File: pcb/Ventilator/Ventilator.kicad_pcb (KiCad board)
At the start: 2 copper layers, 91 parts, among them J2 Screw_Terminal_01x08, J3 Screw_Terminal_01x08, J4 Screw_Terminal_01x02, K1 FINDER-40.52.7.012.0000, K2 FINDER-40.52.7.012.0000, K3 FINDER-40.52.7.012.0000, Q1 NUD3160, Q2 NUD3160, Q3 NUD3160, SW1 Reset, U1 W25Q128JVS, U2 RP2040, U3 4N25, U4 4N25, U5 4N25, U6 4N25, U7 NCP1117-3.3_SOT223

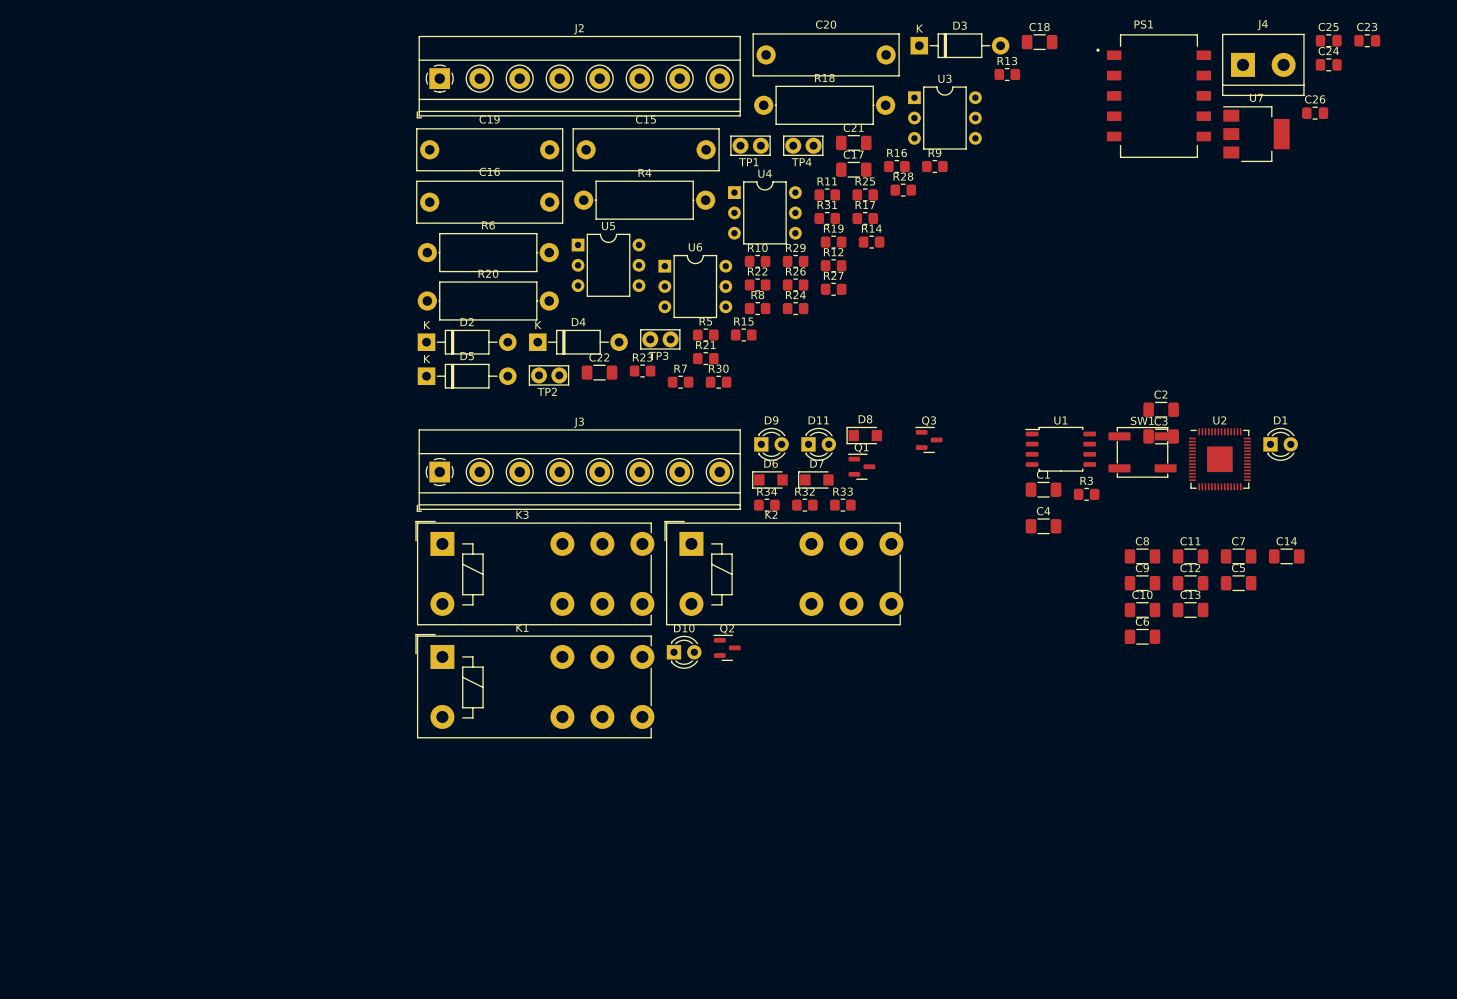
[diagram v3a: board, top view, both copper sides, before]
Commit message: - all parts connected, placed partially
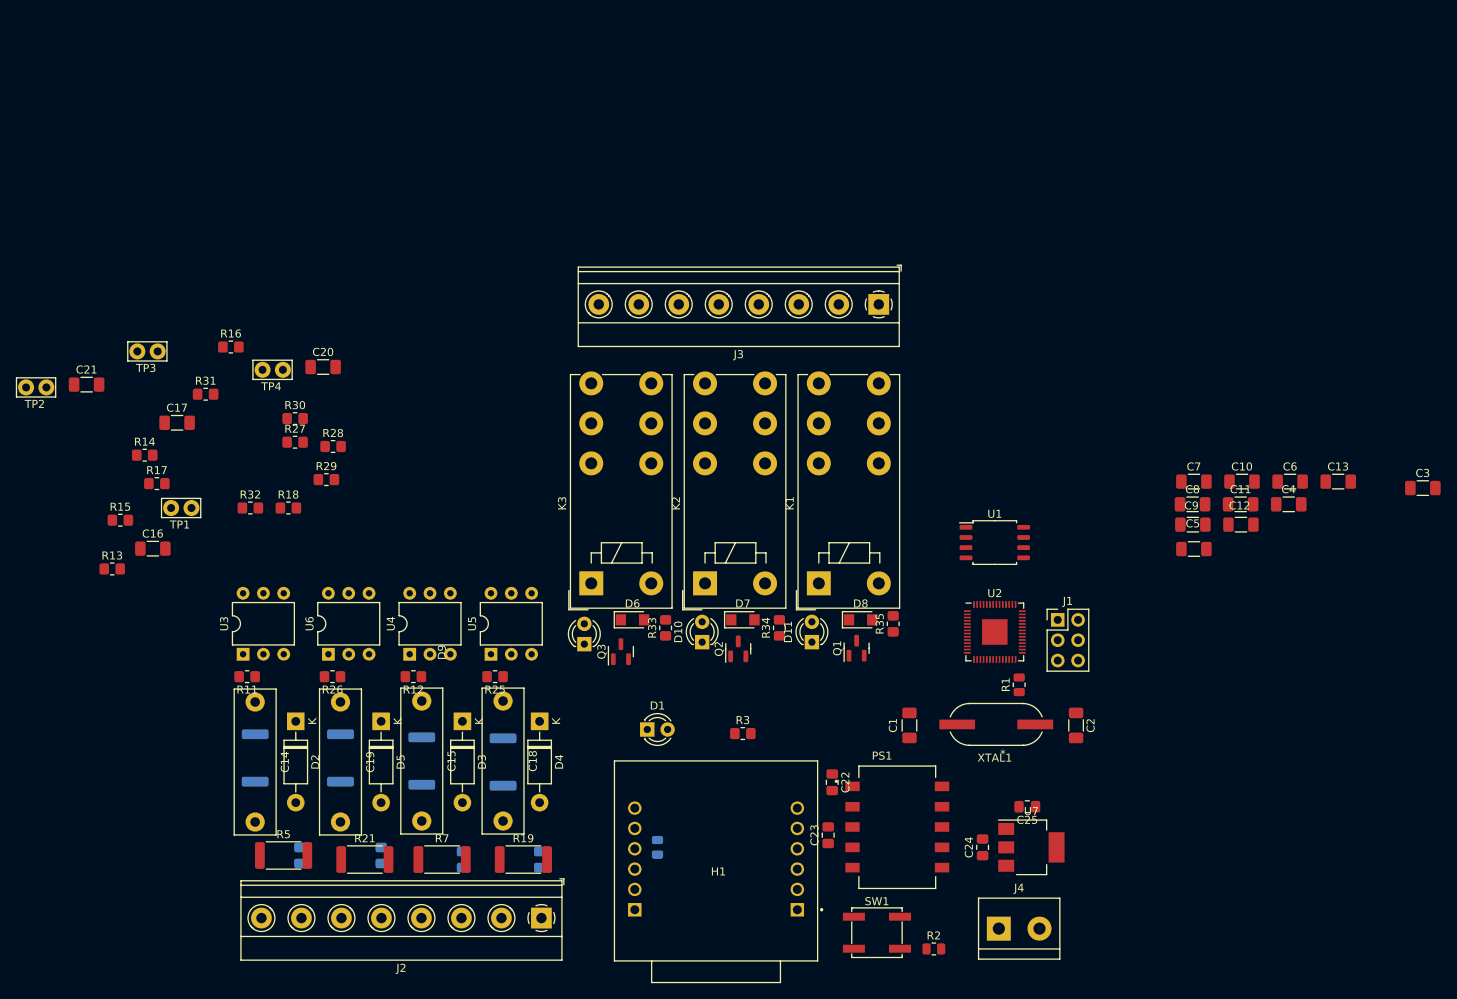
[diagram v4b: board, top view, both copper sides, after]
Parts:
- removed the C1 at (140.2, 127.0)
- added H1: WIZ850IO, W5500:WIZ850IO, F.Cu at (99.6, 174.8)
- added J1: Conn_02x03_Top_Bottom, Connector_PinHeader_2.54mm:PinHeader_2x03_P2.54mm_Vertical, F.Cu at (142.0, 143.3)
- added R1: 1k, Resistor_SMD:R_0805_2012Metric, F.Cu at (137.2, 151.4)
- added R2: 1k, Resistor_SMD:R_0805_2012Metric, F.Cu at (126.5, 184.4)
- added R4: 10k, Resistor_SMD:R_0805_2012Metric, B.Cu at (91.9, 171.7)
- added XTAL1: , Xtal:ABLS-12.000MHZ-B4-T, F.Cu at (134.3, 156.3)
- R10: renamed from R9; footprint Resistor_SMD:R_0805_2012Metric_Pad1.20x1.40mm_HandSolder -> Resistor_SMD:R_2512_6332Metric; moved to B.Cu
- R19: renamed from R18; footprint Resistor_THT:R_Axial_DIN0414_L11.9mm_D4.5mm_P15.24mm_Horizontal -> Resistor_SMD:R_2512_6332Metric
- R20: renamed from R19; moved to B.Cu
- R21: renamed from R20; footprint Resistor_THT:R_Axial_DIN0414_L11.9mm_D4.5mm_P15.24mm_Horizontal -> Resistor_SMD:R_2512_6332Metric
- R22: renamed from R21; moved to B.Cu
- R23: renamed from R22; footprint Resistor_SMD:R_0805_2012Metric_Pad1.20x1.40mm_HandSolder -> Resistor_SMD:R_2512_6332Metric; moved to B.Cu
- R24: renamed from R23; footprint Resistor_SMD:R_0805_2012Metric_Pad1.20x1.40mm_HandSolder -> Resistor_SMD:R_2512_6332Metric; moved to B.Cu
- R5: renamed from R4; footprint Resistor_THT:R_Axial_DIN0414_L11.9mm_D4.5mm_P15.24mm_Horizontal -> Resistor_SMD:R_2512_6332Metric
- R6: renamed from R5; moved to B.Cu
- R7: renamed from R6; footprint Resistor_THT:R_Axial_DIN0414_L11.9mm_D4.5mm_P15.24mm_Horizontal -> Resistor_SMD:R_2512_6332Metric
- R8: renamed from R7; moved to B.Cu
- R9: renamed from R8; footprint Resistor_SMD:R_0805_2012Metric_Pad1.20x1.40mm_HandSolder -> Resistor_SMD:R_2512_6332Metric; moved to B.Cu
- moved R14 117.8 mm to (27.9, 122.7)
- moved C17 117.8 mm to (31.9, 118.6)
- moved C23 114.8 mm to (113.3, 170.2), turned to 90 degrees
- moved C22 114.3 mm to (113.8, 163.6), turned to -90 degrees
- moved J4 112.2 mm to (134.6, 181.9)
- moved C24 109.7 mm to (132.6, 171.7), turned to 90 degrees
- moved U3 109.0 mm to (40.1, 147.6), turned to 90 degrees
- moved J2 105.7 mm to (77.4, 180.5), turned to 180 degrees
- moved D3 102.0 mm to (67.6, 156.0), turned to -90 degrees
- moved R17 100.6 mm to (29.4, 126.2)
- moved R15 100.1 mm to (24.8, 130.8)
- moved C16 99.6 mm to (28.9, 134.4)
- moved R19 98.9 mm to (75.2, 173.2)
- moved R10 98.2 mm to (62.5, 160.9), turned to -90 degrees
- moved R13 97.8 mm to (23.8, 136.9)
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- renumbered C2 to C1, C11 to C10, C12 to C11, C13 to C12, C14 to C13, C15 to C14, C16 to C15, C17 to C16, C18 to C17, C19 to C18, C20 to C19, C3 to C2, C21 to C20, C22 to C21, C23 to C22, C24 to C23, C25 to C24, C26 to C25, C4 to C3, C5 to C4, C6 to C5, C7 to C6, C8 to C7, C9 to C8, C10 to C9, R10 to R11, R11 to R12, R12 to R13, R13 to R14, R14 to R15, R15 to R16, R16 to R17, R17 to R18, R24 to R25, R25 to R26, R26 to R27, R27 to R28, R28 to R29, R29 to R30, R30 to R31, R31 to R32, R32 to R33, R33 to R34, R34 to R35
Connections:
- C22 pad 1: Net-(C23-Pad1) -> +12V
- D10 pad 2: VCC -> +12V
- D11 pad 2: VCC -> +12V
- D6 pad 1: VCC -> +12V
- D7 pad 1: VCC -> +12V
- D8 pad 1: VCC -> +12V
- D9 pad 2: VCC -> +12V
- J4 pad 2: Net-(C23-Pad1) -> +12V
- K1 pad A1: VCC -> +12V
- K2 pad A1: VCC -> +12V
- K3 pad A1: VCC -> +12V
- PS1 pad 1: Net-(C23-Pad1) -> +12V
- PS1 pad 2: Net-(C23-Pad1) -> +12V
- U2 pad 24: unconnected-(U2-Pad24) -> /CPU/SWCLK
- U2 pad 25: unconnected-(U2-Pad25) -> /CPU/SWD
- U2 pad 27: unconnected-(U2-Pad27) -> /CPU/MISO
- U2 pad 28: unconnected-(U2-Pad28) -> /CPU/SCNN
- U2 pad 29: unconnected-(U2-Pad29) -> /CPU/SCLK
- U2 pad 3: unconnected-(U2-Pad3) -> /CPU/RX
- U2 pad 30: unconnected-(U2-Pad30) -> /CPU/MOSI
- U2 pad 31: unconnected-(U2-Pad31) -> /CPU/RSTN

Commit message: - voor omschakeling naar rp pico
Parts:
- removed the C10 at (165.0, 126.0)
- added D12: BAT760,115, Diode_SMD:D_SOD-323_HandSoldering, F.Cu at (133.5, 177.5)
- C10: renamed from C11; footprint Capacitor_SMD:C_1206_3216Metric_Pad1.33x1.80mm_HandSolder -> Capacitor_SMD:C_0805_2012Metric_Pad1.18x1.45mm_HandSolder; moved to B.Cu
- C11: renamed from C12; footprint Capacitor_SMD:C_1206_3216Metric_Pad1.33x1.80mm_HandSolder -> Capacitor_SMD:C_0805_2012Metric_Pad1.18x1.45mm_HandSolder; moved to B.Cu
- C12: renamed from C13; footprint Capacitor_SMD:C_1206_3216Metric_Pad1.33x1.80mm_HandSolder -> Capacitor_SMD:C_0805_2012Metric_Pad1.18x1.45mm_HandSolder; moved to B.Cu
- C21: renamed from C22; moved to B.Cu
- C22: renamed from C23; moved to B.Cu
- C3, C4, C5, C6, C7, C8, C9: footprint Capacitor_SMD:C_1206_3216Metric_Pad1.33x1.80mm_HandSolder -> Capacitor_SMD:C_0805_2012Metric_Pad1.18x1.45mm_HandSolder; moved to B.Cu
- D6, D7, D8, Q1, Q2, Q3, R11, R12, R25, R26: moved to B.Cu
- R2: value 1k -> 10k
- XTAL1: value (none) -> ABLS-12.000MHZ-B4-T
- moved D8 80.9 mm to (39.6, 120.9), turned to -90 degrees
- moved C3 66.7 mm to (124.1, 147.2)
- moved C10 58.2 mm to (108.6, 143.6), turned to 180 degrees
- moved C12 56.3 mm to (124.1, 145.2)
- moved C23 53.6 mm to (83.8, 149.4)
- moved U8 53.2 mm to (90.4, 149.4)
- moved C6 52.4 mm to (124.1, 149.4)
- moved C5 51.7 mm to (108.6, 145.8)
- moved TP2 51.0 mm to (61.7, 129.5)
- moved C24 49.3 mm to (90.4, 154.4)
- moved C4 48.9 mm to (124.1, 143.1), turned to 180 degrees
- moved TP3 48.2 mm to (70.9, 129.5)
- moved Q3 47.6 mm to (47.8, 120.9), turned to 180 degrees
- moved C9 47.5 mm to (115.8, 151.5), turned to -90 degrees
- moved C7 47.0 mm to (119.5, 151.5), turned to -90 degrees
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- renumbered C14 to C13, C15 to C14, C16 to C15, C17 to C16, C18 to C17, C19 to C18, C20 to C19, C21 to C20, C24 to C23, C25 to C24, U3 to U4, U4 to U5, U5 to U6, U6 to U7, U7 to U8
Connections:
- net Net-(C3-Pad1) renamed +1V1
- J4 pad 2: +12V -> Net-(D12-Pad2)
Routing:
- net +3.3V: track 0.00 -> 45.5 mm, vias 0 -> 4
- net +1V1: track 0.00 -> 25.2 mm, vias 0 -> 3
- net Net-(C1-Pad1): track 0.00 -> 14.8 mm
- net Net-(C2-Pad1): track 0.00 -> 9.91 mm
- net Net-(R1-Pad2): track 0.00 -> 7.70 mm

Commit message: - voor autorouter
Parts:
- removed the C1 at (100.1, 141.7)
- removed the C10 at (108.6, 143.6)
- removed C11, C12: 100n, Capacitor_SMD:C_0805_2012Metric_Pad1.18x1.45mm_HandSolder
- removed the C2 at (100.1, 148.8)
- removed C23, C24: 10u, Capacitor_SMD:C_0805_2012Metric_Pad1.18x1.45mm_HandSolder
- removed the C3 at (124.1, 147.2)
- removed the C4 at (124.1, 143.1)
- removed the C5 at (108.6, 145.8)
- removed the C6 at (124.1, 149.4)
- removed the C7 at (119.5, 151.5)
- removed the C8 at (115.8, 137.0)
- removed the C9 at (115.8, 151.5)
- removed the R1 at (109.9, 149.7)
- removed the U2 at (116.8, 144.3)
- removed U8: NCP1117-3.3_SOT223, Package_TO_SOT_SMD:SOT-223-3_TabPin2
- removed XTAL1: ABLS-12.000MHZ-B4-T, Xtal:ABLS-12.000MHZ-B4-T
- added JP1: SolderJumper_3_Bridged12, Jumper:SolderJumper-3_P1.3mm_Bridged12_Pad1.0x1.5mm, F.Cu at (135.9, 130.2)
- PS1: value R-78AA3.3-0.5SMD-R -> R-78AA5.0-0.5SMD-R
- U1: value W25Q128JVS -> Pico; footprint Package_SO:SOIC-8_5.23x5.23mm_P1.27mm -> MCU_RaspberryPi_and_Boards:RPi_Pico_SMD_TH
- moved D7 58.9 mm to (77.2, 121.2), turned to -90 degrees
- moved D6 50.4 mm to (124.1, 121.2), turned to 90 degrees
- moved R32 41.6 mm to (135.0, 108.3)
- moved D9 41.6 mm to (136.0, 105.5)
- moved R33 27.3 mm to (127.8, 108.3)
- moved D10 27.3 mm to (128.8, 105.5)
- moved R3 16.9 mm to (120.8, 167.3)
- moved R34 14.1 mm to (120.5, 108.3)
- moved D11 14.1 mm to (121.5, 105.5)
- moved U1 13.5 mm to (113.0, 144.4)
- moved TP2 6.00 mm to (65.4, 134.2), turned to 90 degrees
- moved D8 5.97 mm to (45.6, 121.2)
- moved TP1 5.81 mm to (45.1, 134.4), turned to 90 degrees
- moved TP3 5.07 mm to (75.4, 131.7), turned to -90 degrees
- moved R1 4.19 mm to (86.4, 172.2), turned to 0 degrees
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- renumbered C13 to C1, C22 to C10, C14 to C2, C15 to C3, C16 to C4, C17 to C5, C18 to C6, C19 to C7, C20 to C8, C21 to C9, R3 to R1, R11 to R10, R12 to R11, R13 to R12, R14 to R13, R15 to R14, R16 to R15, R17 to R16, R18 to R17, R19 to R18, R20 to R19, R4 to R2, R21 to R20, R22 to R21, R23 to R22, R24 to R23, R25 to R24, R26 to R25, R27 to R26, R28 to R27, R29 to R28, R30 to R29, R2 to R3, R31 to R30, R32 to R31, R33 to R32, R34 to R33, R35 to R34, R5 to R4, R6 to R5, R7 to R6, R8 to R7, R9 to R8, R10 to R9, U4 to U2, U5 to U3, U6 to U4, U7 to U5
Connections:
- C10 pad 1: VCC -> +5V
- J3 pad 2: Net-(J3-Pad2) -> Net-(K1-Pad11)
- J3 pad 3: Net-(J3-Pad3) -> Net-(K2-Pad14)
- J3 pad 4: Net-(J3-Pad4) -> Net-(K2-Pad11)
- J3 pad 5: Net-(J3-Pad5) -> Net-(K3-Pad14)
- J3 pad 6: Net-(J3-Pad6) -> Net-(K3-Pad11)
- K1 pad 11: unconnected-(K1-Pad11) -> Net-(K1-Pad11)
- K1 pad 14: unconnected-(K1-Pad14) -> Net-(J3-Pad1)
- K1 pad 21: Net-(J3-Pad2) -> Net-(K1-Pad11)
- K2 pad 11: unconnected-(K2-Pad11) -> Net-(K2-Pad11)
- K2 pad 14: unconnected-(K2-Pad14) -> Net-(K2-Pad14)
- K2 pad 21: Net-(J3-Pad4) -> Net-(K2-Pad11)
- K2 pad 24: Net-(J3-Pad3) -> Net-(K2-Pad14)
- K3 pad 11: unconnected-(K3-Pad11) -> Net-(K3-Pad11)
- K3 pad 14: unconnected-(K3-Pad14) -> Net-(K3-Pad14)
- K3 pad 21: Net-(J3-Pad6) -> Net-(K3-Pad11)
- K3 pad 24: Net-(J3-Pad5) -> Net-(K3-Pad14)
- PS1 pad 4: VCC -> +5V
- PS1 pad 5: VCC -> +5V
- Q2 pad 1: /CPU/OUT3 -> /CPU/OUT2
- Q3 pad 1: /CPU/OUT2 -> /CPU/OUT3
- R1 pad 2: VCC -> +3.3V
- R3 pad 1: Net-(R2-Pad1) -> Net-(R3-Pad1)
- SW1 pad 2: Net-(R2-Pad1) -> Net-(R3-Pad1)
- U1 pad 3: Net-(U1-Pad3) -> GND
- U1 pad 4: GND -> Net-(D1-Pad1)
- U1 pad 5: Net-(U1-Pad5) -> /CPU/IN1
- U1 pad 6: Net-(U1-Pad6) -> /CPU/IN2
- U1 pad 7: Net-(U1-Pad7) -> /CPU/IN3
- U1 pad 8: +3.3V -> GND
- U2 pad 5: VCC -> +3.3V
- U3 pad 5: VCC -> +3.3V
- U4 pad 5: VCC -> +3.3V
- U5 pad 5: VCC -> +3.3V
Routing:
- net Net-(K1-Pad11): track 0.00 -> 56.1 mm
- net +3.3V: track 45.5 -> 0.00 mm, vias 4 -> 0
- net Net-(K2-Pad14): track 0.00 -> 44.7 mm
- net Net-(K2-Pad11): track 0.00 -> 43.5 mm
- net Net-(J3-Pad1): track 0.00 -> 39.6 mm
- net +1V1: track 25.2 -> 0.00 mm, vias 3 -> 0
- net Net-(D4-Pad2): track 0.00 -> 24.3 mm
- net Net-(D3-Pad2): track 0.00 -> 24.1 mm
- net Net-(D5-Pad2): track 0.00 -> 24.0 mm
- net Net-(D2-Pad2): track 0.00 -> 24.0 mm
- net Net-(K3-Pad14): track 0.00 -> 21.5 mm
- net Net-(K3-Pad11): track 0.00 -> 21.5 mm
- net Net-(R12-Pad1): track 0.00 -> 15.1 mm
- net Net-(C1-Pad1) (its old number): track 14.8 -> 0.00 mm
- net Net-(R27-Pad1): track 0.00 -> 14.7 mm
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
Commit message: - as ordered (30/12/2022)
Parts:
- moved R3 3.92 mm to (120.9, 171.2)
- moved R10 2.49 mm to (40.8, 151.4)
- moved R19 2.43 mm to (78.4, 171.4)
- moved R25 2.38 mm to (50.8, 151.4)
- moved R18 2.18 mm to (76.1, 171.4)
- moved R11 2.17 mm to (60.8, 151.4)
- moved J1 2.15 mm to (134.7, 118.5)
- moved R24 2.01 mm to (70.8, 151.4)
- moved JP1 1.78 mm to (135.9, 128.4)
- moved D3 1.67 mm to (68.4, 154.9)
- moved D2 1.67 mm to (48.4, 154.9)
- moved C5 1.67 mm to (73.4, 152.4)
- moved D4 1.67 mm to (78.4, 154.9)
- moved R22 1.67 mm to (73.4, 159.9)
- moved R7 1.67 mm to (68.4, 171.4)
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- renumbered K3 to locked, J3 to locked, D11 to locked, C1 to locked
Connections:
- net Net-(J3-Pad1) renamed /Output/220_1
- net Net-(K1-Pad11) renamed /Output/220_2
- net Net-(K2-Pad11) renamed /Output/220_4
- net Net-(K2-Pad14) renamed /Output/220_3
- net Net-(K3-Pad11) renamed /Output/220_6
- net Net-(K3-Pad14) renamed /Output/220_5
- U1 pad 11: /CPU/OUT2 -> unconnected-(U1-Pad11)
- U1 pad 19: unconnected-(U1-Pad19) -> /CPU/OUT2
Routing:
- net GND: track 0.00 -> 335.8 mm
- net +12V: track 13.9 -> 247.5 mm
- net +3.3V: track 0.00 -> 177.0 mm
- net Net-(D8-Pad2): track 0.05 -> 108.2 mm
- net /CPU/IN1: track 0.22 -> 105.6 mm
- net Net-(D7-Pad2): track 0.70 -> 87.0 mm, vias 1 -> 0
- net /CPU/IN2: track 0.18 -> 81.9 mm
- net Net-(D1-Pad1): track 0.00 -> 73.0 mm
- net /CPU/IN3: track 0.27 -> 72.2 mm
- net /CPU/SWCLK: track 0.00 -> 63.0 mm
- net /CPU/SWD: track 0.00 -> 60.6 mm
- net Net-(R3-Pad1): track 0.00 -> 58.4 mm
- net /CPU/IN4: track 0.00 -> 52.6 mm
- net /CPU/OUT3: track 0.00 -> 48.7 mm
- net /CPU/SCNN: track 0.00 -> 33.1 mm
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- added copper zone on B.Cu, net GND
- added copper zone on F.Cu, net GND
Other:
- board outline added: 103 x 86.5 mm
